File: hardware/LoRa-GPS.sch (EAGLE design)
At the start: 26 parts, among them J2 MF-CON-MICROUSB-RIGHT, U1 MCP1703-3302E/CB, Y1 CRYSTAL.ABS07

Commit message: tidy
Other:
- moved on the sheet: C4, C5
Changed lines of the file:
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@@
 <part name="FRAME2" library="frames" library_urn="urn:adsk.eagle:library:229" deviceset="FRAME_B_L" device=""/>
 <part name="TP1" library="SparkFun-Passives" deviceset="TEST-POINT" device="3X5" value="GND"/>
+<part name="GND3" library="supply1" deviceset="GND" device=""/>
 </parts>
 <sheets>
@@
 <attribute name="VALUE" x="-233.68" y="96.52" size="1.778" layer="96"/>
 </instance>
-<instance part="C4" gate="G$1" x="-132.08" y="83.82" smashed="yes" rot="R90">
-<attribute name="NAME" x="-132.461" y="85.344" size="1.778" layer="95" rot="R90"/>
-<attribute name="VALUE" x="-127.381" y="85.344" size="1.778" layer="96" rot="R90"/>
-</instance>
-<instance part="C5" gate="G$1" x="-144.78" y="86.36" smashed="yes" rot="R90">
-<attribute name="NAME" x="-145.161" y="87.884" size="1.778" layer="95" rot="R90"/>
-<attribute name="VALUE" x="-140.081" y="87.884" size="1.778" layer="96" rot="R90"/>
+<instance part="C4" gate="G$1" x="-119.38" y="76.2" smashed="yes">
+<attribute name="NAME" x="-117.856" y="76.581" size="1.778" layer="95"/>
+<attribute name="VALUE" x="-117.856" y="71.501" size="1.778" layer="96"/>
+</instance>
+<instance part="C5" gate="G$1" x="-127" y="76.2" smashed="yes">
+<attribute name="NAME" x="-125.476" y="76.581" size="1.778" layer="95"/>
+<attribute name="VALUE" x="-125.476" y="71.501" size="1.778" layer="96"/>
 </instance>
 <instance part="C6" gate="G$1" x="-215.9" y="68.58" smashed="yes" rot="R90">
@@
 <attribute name="VALUE" x="-220.98" y="60.96" size="1.778" layer="96"/>
 </instance>
-<instance part="GND5" gate="1" x="-139.7" y="78.74" smashed="yes">
-<attribute name="VALUE" x="-142.24" y="76.2" size="1.778" layer="96"/>
+<instance part="GND5" gate="1" x="-127" y="68.58" smashed="yes">
+<attribute name="VALUE" x="-129.54" y="66.04" size="1.778" layer="96"/>
 </instance>
 <instance part="GND7" gate="1" x="-238.76" y="83.82" smashed="yes">
 <attribute name="VALUE" x="-241.3" y="81.28" size="1.778" layer="96"/>
 </instance>
-<instance part="GND8" gate="1" x="-124.46" y="81.28" smashed="yes">
-<attribute name="VALUE" x="-127" y="78.74" size="1.778" layer="96"/>
+<instance part="GND8" gate="1" x="-119.38" y="68.58" smashed="yes">
+<attribute name="VALUE" x="-121.92" y="66.04" size="1.778" layer="96"/>
 </instance>
 <instance part="P+1" gate="VCC" x="-205.74" y="-106.68" smashed="yes">
 <attribute name="VALUE" x="-208.28" y="-109.22" size="1.778" layer="96" rot="R180"/>
 </instance>
-<instance part="P+2" gate="VCC" x="-147.32" y="101.6" smashed="yes">
-<attribute name="VALUE" x="-149.86" y="99.06" size="1.778" layer="96" rot="R90"/>
+<instance part="P+2" gate="VCC" x="-127" y="96.52" smashed="yes">
+<attribute name="VALUE" x="-129.54" y="93.98" size="1.778" layer="96" rot="R90"/>
 </instance>
 <instance part="GND9" gate="1" x="-254" y="-137.16" smashed="yes">
@@
 <attribute name="NAME" x="-218.44" y="2.54" size="1.778" layer="95"/>
 <attribute name="VALUE" x="-218.44" y="-2.54" size="1.778" layer="96"/>
+</instance>
+<instance part="GND3" gate="1" x="-137.16" y="68.58" smashed="yes">
+<attribute name="VALUE" x="-139.7" y="66.04" size="1.778" layer="96"/>
 </instance>
 </instances>
@@
 <pinref part="GND8" gate="1" pin="GND"/>
 <pinref part="C4" gate="G$1" pin="2"/>
-<wire x1="-124.46" y1="83.82" x2="-127" y2="83.82" width="0.1524" layer="91"/>
-</segment>
-<segment>
-<pinref part="SAMD21" gate="G$1" pin="GND@2"/>
+</segment>
+<segment>
 <pinref part="GND5" gate="1" pin="GND"/>
-<wire x1="-165.1" y1="81.28" x2="-139.7" y2="81.28" width="0.1524" layer="91"/>
 <pinref part="C5" gate="G$1" pin="2"/>
-<wire x1="-139.7" y1="86.36" x2="-139.7" y2="81.28" width="0.1524" layer="91"/>
-<junction x="-139.7" y="81.28"/>
 </segment>
 <segment>
@@
 <wire x1="-215.9" y1="0" x2="-223.52" y2="0" width="0.1524" layer="91"/>
 </segment>
-</net>
-<net name="N$5" class="0">
-<segment>
-<pinref part="SAMD21" gate="G$1" pin="VDDCORE"/>
-<pinref part="C4" gate="G$1" pin="1"/>
-<wire x1="-165.1" y1="83.82" x2="-134.62" y2="83.82" width="0.1524" layer="91"/>
+<segment>
+<pinref part="SAMD21" gate="G$1" pin="GND@2"/>
+<wire x1="-165.1" y1="81.28" x2="-137.16" y2="81.28" width="0.1524" layer="91"/>
+<pinref part="GND3" gate="1" pin="GND"/>
+<wire x1="-137.16" y1="81.28" x2="-137.16" y2="71.12" width="0.1524" layer="91"/>
 </segment>
 </net>
@@
 </segment>
 <segment>
+<pinref part="C5" gate="G$1" pin="1"/>
+<pinref part="P+2" gate="VCC" pin="VCC"/>
+<wire x1="-127" y1="93.98" x2="-127" y2="86.36" width="0.1524" layer="91"/>
 <pinref part="SAMD21" gate="G$1" pin="VDDIN"/>
-<pinref part="C5" gate="G$1" pin="1"/>
-<wire x1="-165.1" y1="86.36" x2="-147.32" y2="86.36" width="0.1524" layer="91"/>
-<pinref part="P+2" gate="VCC" pin="VCC"/>
-<wire x1="-147.32" y1="99.06" x2="-147.32" y2="86.36" width="0.1524" layer="91"/>
-<junction x="-147.32" y="86.36"/>
+<wire x1="-127" y1="86.36" x2="-127" y2="78.74" width="0.1524" layer="91"/>
+<wire x1="-165.1" y1="86.36" x2="-127" y2="86.36" width="0.1524" layer="91"/>
+<junction x="-127" y="86.36"/>
 </segment>
 <segment>
@@
 </segment>
 </net>
+<net name="N$5" class="0">
+<segment>
+<pinref part="SAMD21" gate="G$1" pin="VDDCORE"/>
+<wire x1="-165.1" y1="83.82" x2="-119.38" y2="83.82" width="0.1524" layer="91"/>
+<pinref part="C4" gate="G$1" pin="1"/>
+<wire x1="-119.38" y1="83.82" x2="-119.38" y2="78.74" width="0.1524" layer="91"/>
+</segment>
+</net>

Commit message: tinker
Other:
- moved on the sheet: S2

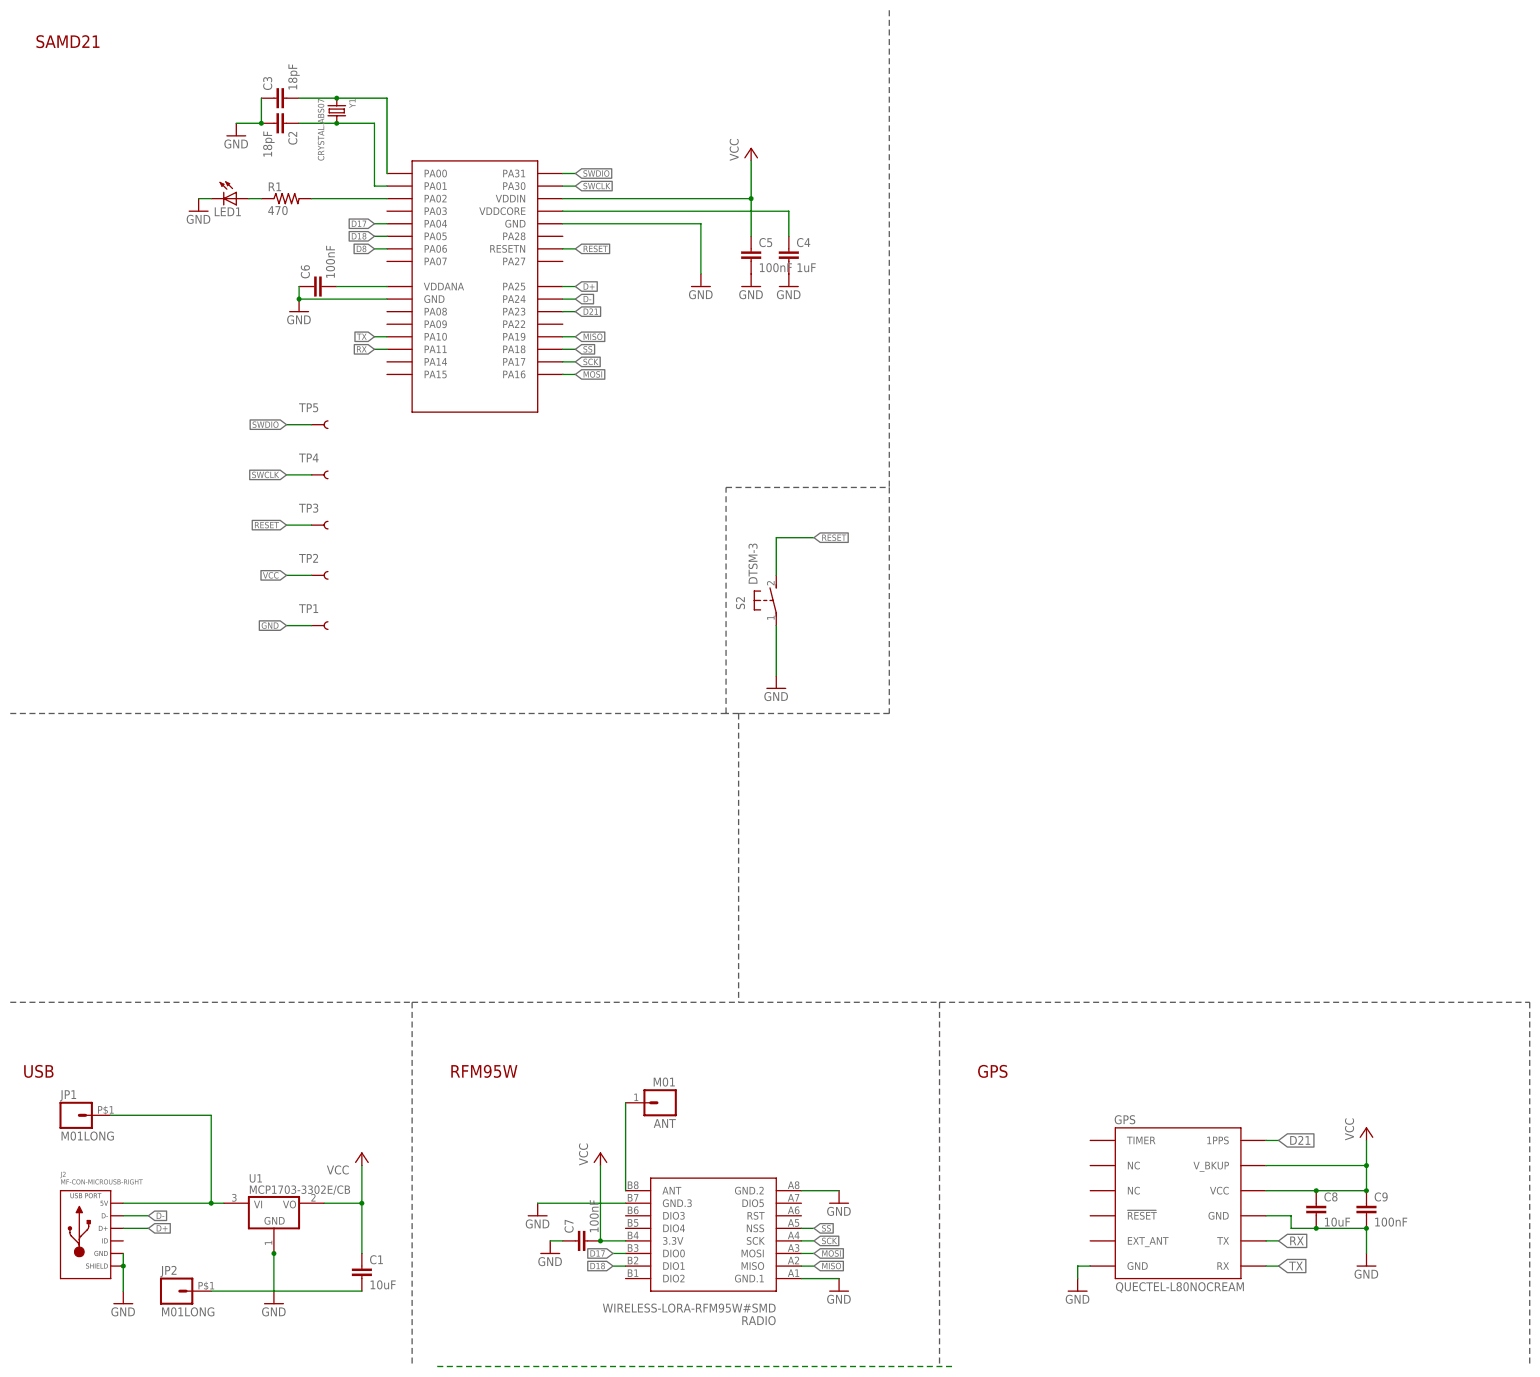
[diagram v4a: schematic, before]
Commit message: add gps power switch
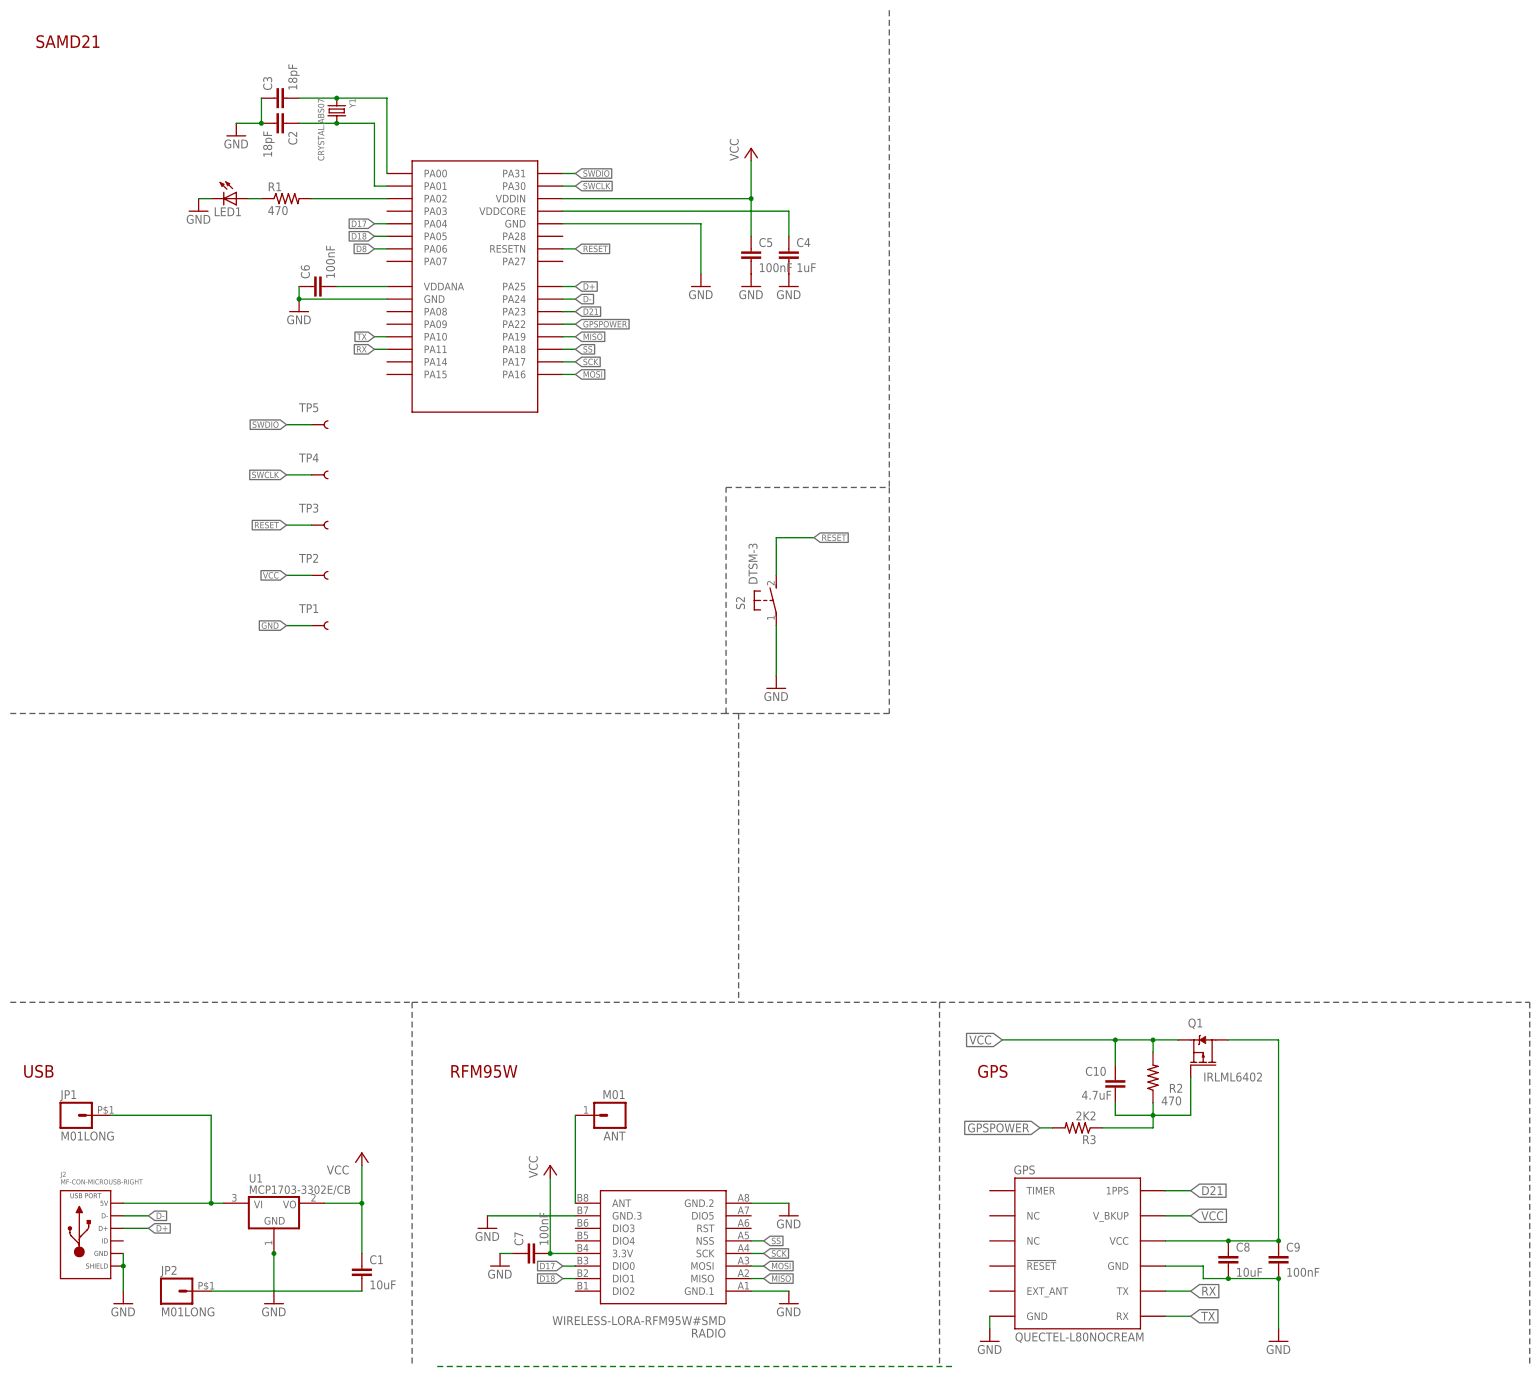
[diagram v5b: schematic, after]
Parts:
- added C10: 4.7uF, nootropicdesign:CAPC0603-THINCREAM
- added Q1: IRLML6402, ianc:MOSFET_PCH-IRLML6402
- added R2: 470, nootropicdesign:R-USR0603-THINCREAM
- added R3: 2K2, nootropicdesign:R-USR0603-THINCREAM
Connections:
- new net GPSPOWER: R3.2, SAMD21.PA22
- new net N$7: C8.1, C9.1, GPS.VCC, Q1.D
- new net N$8: C10.2, Q1.G, R2.1, R3.1
- net VCC: now also C10.1, Q1.S, R2.2; no longer C8.1, C9.1, GPS.VCC
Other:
- moved on the sheet: ANT, C7, C8, C9, GPS, RADIO
